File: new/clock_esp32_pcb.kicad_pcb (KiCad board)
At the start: 2 copper layers, 9 parts

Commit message: added dsn file
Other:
- board outline added: 34 x 44.5 mm
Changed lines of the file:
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@@
 	)
 	(gr_rect
-		(start 34.5 43)
-		(end 71.5 89)
+		(start 36 44.5)
+		(end 70 89)
 		(stroke
-			(width 0.2)
+			(width 0.05)
 			(type default)
 		)
 		(fill no)
-		(layer "F.Cu")
+		(layer "Edge.Cuts")
 	)
 	(embedded_fonts no)

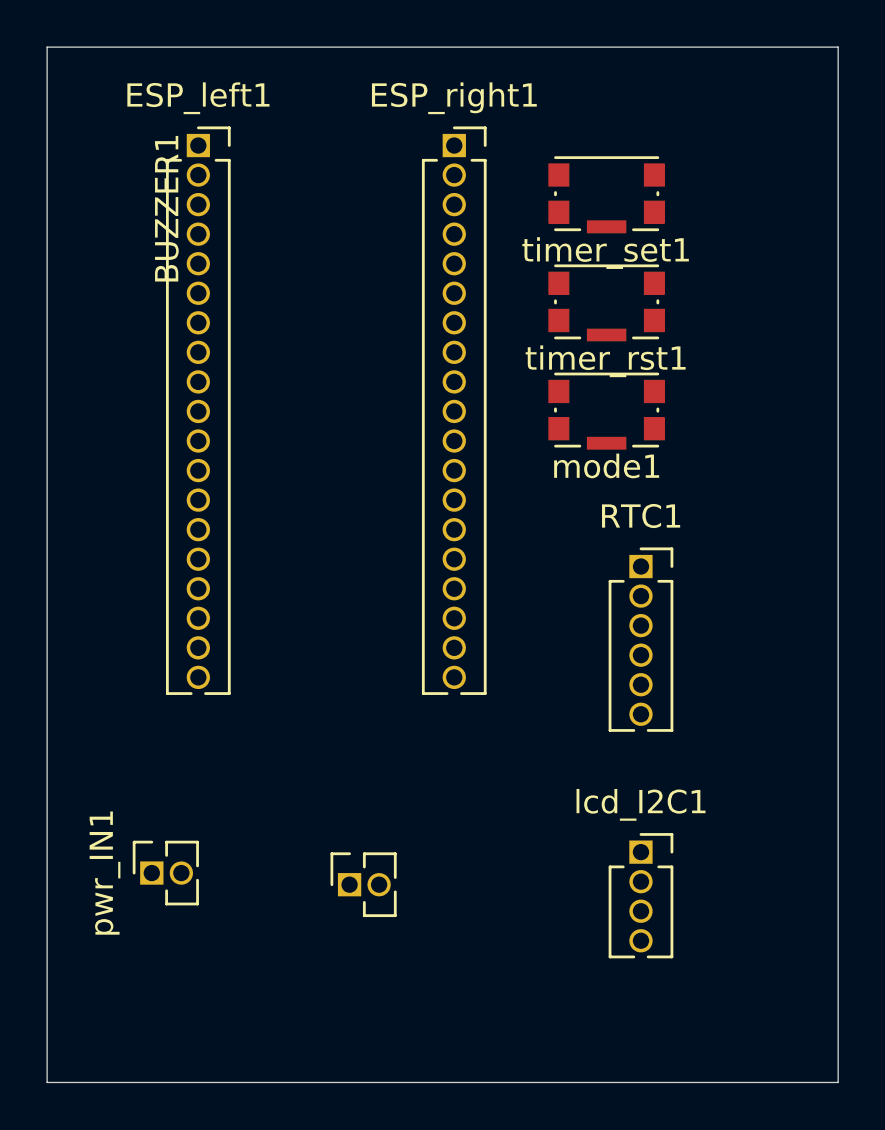
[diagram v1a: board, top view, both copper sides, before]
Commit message: made changes to the final layout (reduced size)
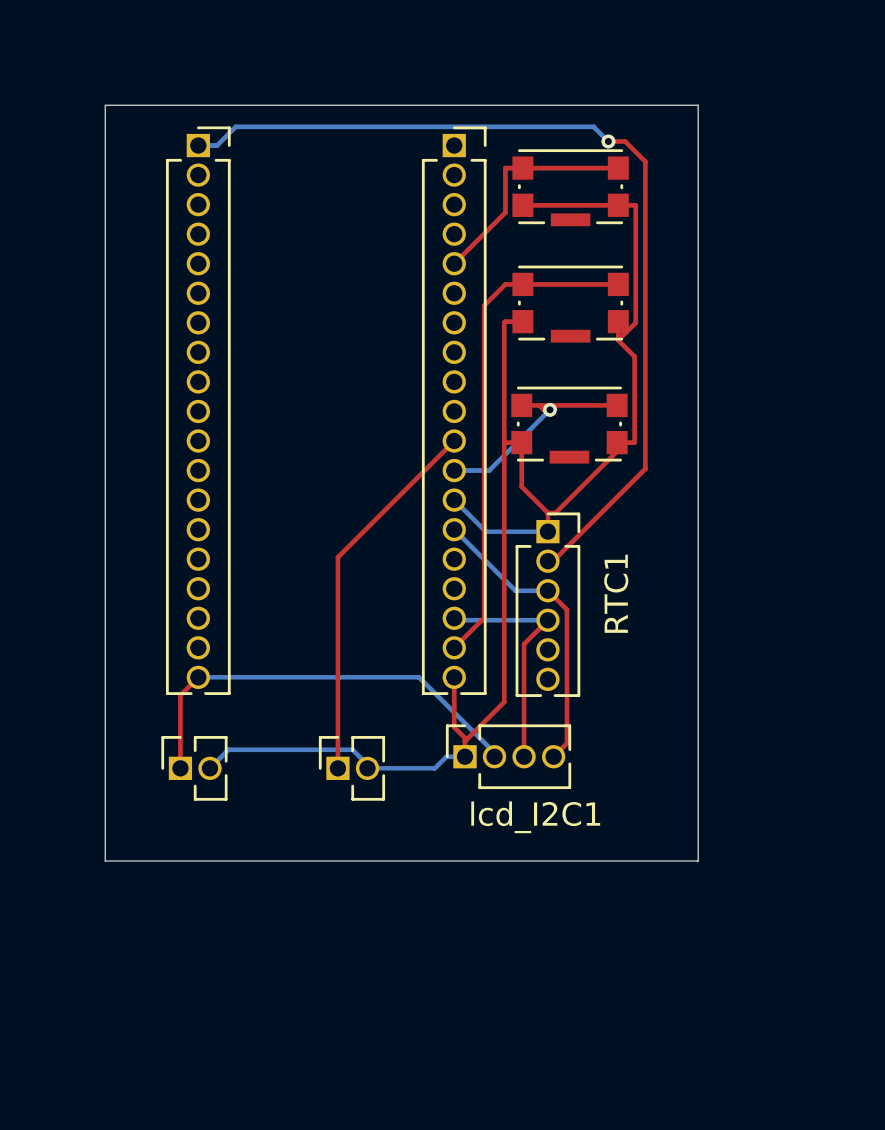
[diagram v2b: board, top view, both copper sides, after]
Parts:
- moved lcd_I2C1 8.60 mm to (54.0, 75.0), turned to 90 degrees
- moved BUZZER1 5.02 mm to (48.5, 75.5)
- moved pwr_IN1 4.67 mm to (41.7, 75.5)
- moved RTC1 4.27 mm to (57.5, 65.3)
- moved mode1 1.71 mm to (58.5, 60.7)
- moved timer_set1 1.58 mm to (58.5, 50.5)
- moved timer_rst1 1.55 mm to (58.5, 55.5)
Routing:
- net GND: track 0.00 -> 66.5 mm
- net +3V3: track 0.00 -> 39.2 mm, vias 0 -> 1
- net Net-(ESP_right1-Pin_18): track 0.00 -> 21.4 mm
- net +5V: track 0.00 -> 18.5 mm
- net Net-(BUZZER1-Pin_1): track 0.00 -> 16.1 mm
- net Net-(ESP_right1-Pin_14): track 0.00 -> 12.8 mm
- net Net-(ESP_right1-Pin_17): track 0.00 -> 10.3 mm
- net Net-(ESP_right1-Pin_5): track 0.00 -> 9.87 mm
- net Net-(ESP_right1-Pin_12): track 0.00 -> 9.83 mm, vias 0 -> 1
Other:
- board size 34 x 44.5 mm -> 25.5 x 32.5 mm
- board text added: "BUZZER"
- board text added: "ESP32-WROOM-32D"
- board text added: "PWR_IN"

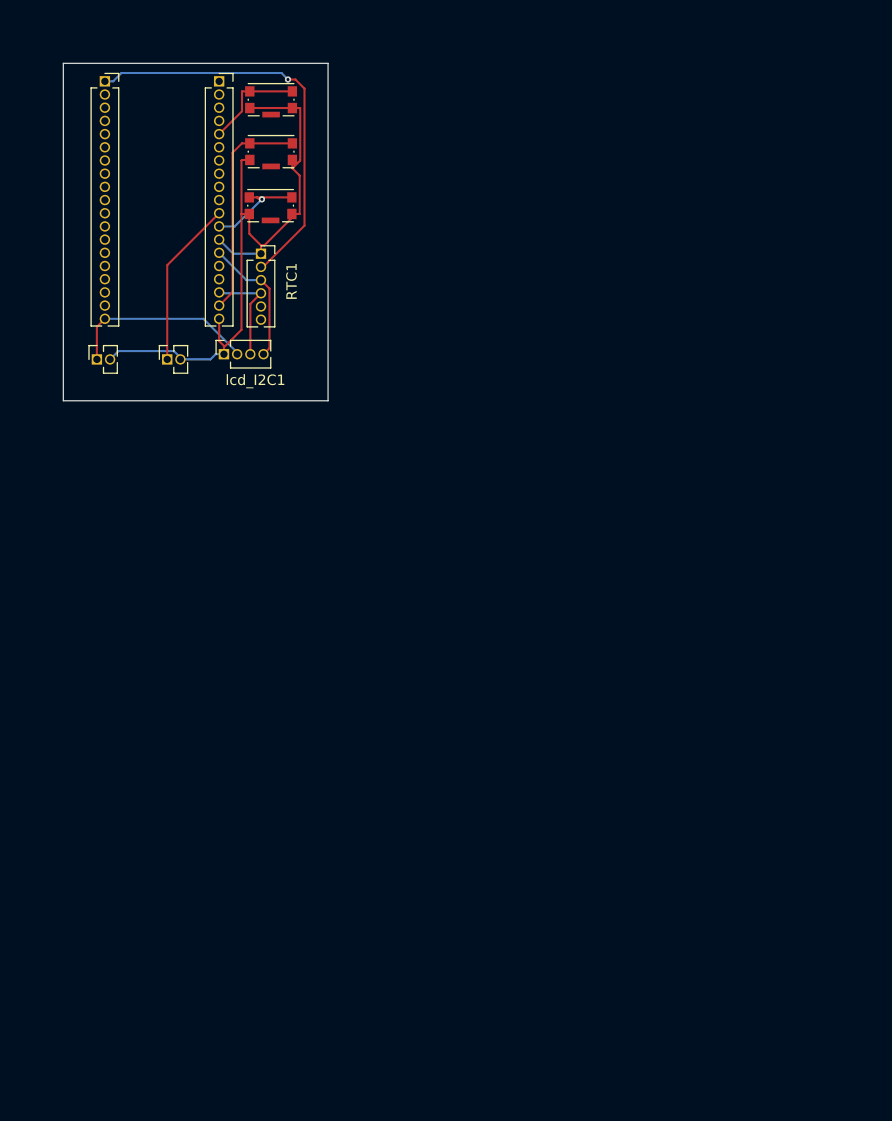
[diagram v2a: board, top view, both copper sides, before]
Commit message: final routing completed
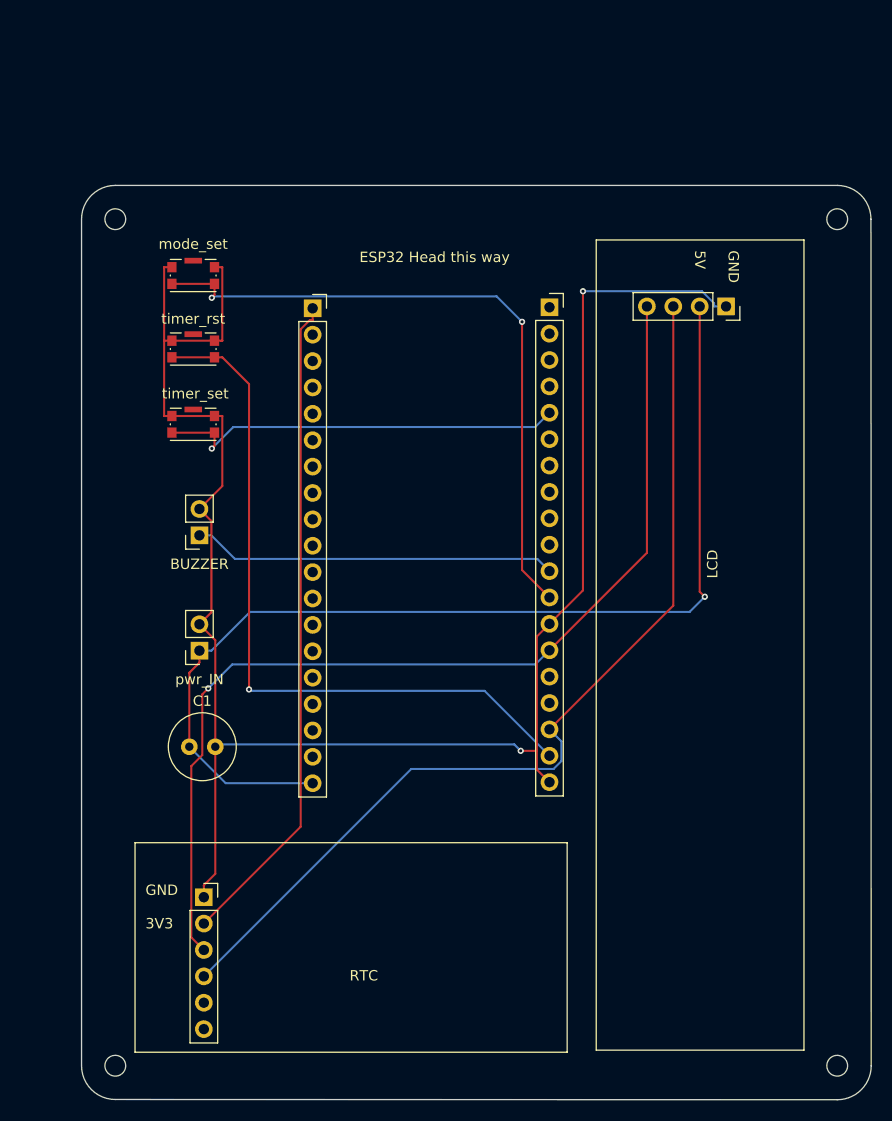
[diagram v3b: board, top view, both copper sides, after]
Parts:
- removed BUZZER1, pwr_IN1: Conn_01x02_Socket, Connector_PinSocket_1.27mm:PinSocket_1x02_P1.27mm_Vertical
- removed RTC1: Conn_01x06, Connector_PinSocket_1.27mm:PinSocket_1x06_P1.27mm_Vertical
- removed lcd_I2C1: Conn_01x04_Socket, Connector_PinSocket_1.27mm:PinSocket_1x04_P1.27mm_Vertical
- removed mode1, timer_rst1, timer_set1: SW_Push, Button_Switch_SMD:SW_Push_1P1T-SH_NO_CK_KMR2xxG
- added BUZZER: Conn_01x02_Socket, Connector_PinSocket_2.54mm:PinSocket_1x02_P2.54mm_Vertical, F.Cu at (51.6, 92.4)
- added C1: C, Capacitor_THT:C_Radial_D6.3mm_H5.0mm_P2.50mm, F.Cu at (50.6, 112.8)
- added LCD: Conn_01x04_Socket, Connector_PinSocket_2.54mm:PinSocket_1x04_P2.54mm_Vertical, F.Cu at (102.3, 70.4)
- added RTC: Conn_01x06, Connector_PinSocket_2.54mm:PinSocket_1x06_P2.54mm_Vertical, F.Cu at (52.0, 127.3)
- added mode_set: SW_Push, Button_Switch_SMD:SW_Push_1P1T-SH_NO_CK_KMR2xxG, F.Cu at (51.0, 67.4)
- added pwr_IN: Conn_01x02_Socket, Connector_PinSocket_2.54mm:PinSocket_1x02_P2.54mm_Vertical, F.Cu at (51.6, 103.5)
- added timer_rst: SW_Push, Button_Switch_SMD:SW_Push_1P1T-SH_NO_CK_KMR2xxG, F.Cu at (51.0, 74.5)
- added timer_set: SW_Push, Button_Switch_SMD:SW_Push_1P1T-SH_NO_CK_KMR2xxG, F.Cu at (51.0, 81.8)
- ESP_left1, ESP_right1: footprint Connector_PinSocket_1.27mm:PinSocket_1x19_P1.27mm_Vertical -> Connector_PinSocket_2.54mm:PinSocket_1x19_P2.54mm_Vertical
- moved ESP_right1 38.5 mm to (85.3, 70.5)
- moved ESP_left1 29.6 mm to (62.5, 70.6)
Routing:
- net GND: track 66.5 -> 178.8 mm, vias 0 -> 2
- net Net-(ESP_right1-Pin_14): track 12.8 -> 97.7 mm, vias 0 -> 1
- net +5V: track 18.5 -> 101.9 mm, vias 0 -> 1
- net Net-(ESP_right1-Pin_17): track 10.3 -> 92.2 mm
- net Net-(ESP_right1-Pin_12): track 9.83 -> 64.1 mm, vias 1 -> 2
- net Net-(ESP_right1-Pin_18): track 21.4 -> 69.5 mm, vias 0 -> 1
- net Net-(ESP_right1-Pin_5): track 9.87 -> 39.7 mm, vias 0 -> 1
- net +3V3: track 39.2 -> 63.7 mm, vias 1 -> 0
- net Net-(BUZZER1-Pin_1): track 16.1 -> 35.1 mm
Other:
- board size 25.5 x 32.5 mm -> 76 x 88 mm
- board text added: "ESP32 Head this way"
- board text added: "GND 3V3"
- board text added: "GND 5V"
- board text removed: "BUZZER"
- board text removed: "ESP32-WROOM-32D"
- board text removed: "PWR_IN"
